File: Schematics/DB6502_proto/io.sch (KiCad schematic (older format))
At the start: 21 parts, among them J7 UART A, J8 UART_A, U17 SC26C92, U18 FT230XS, U4 74AC04, Y2 3,6864MHz

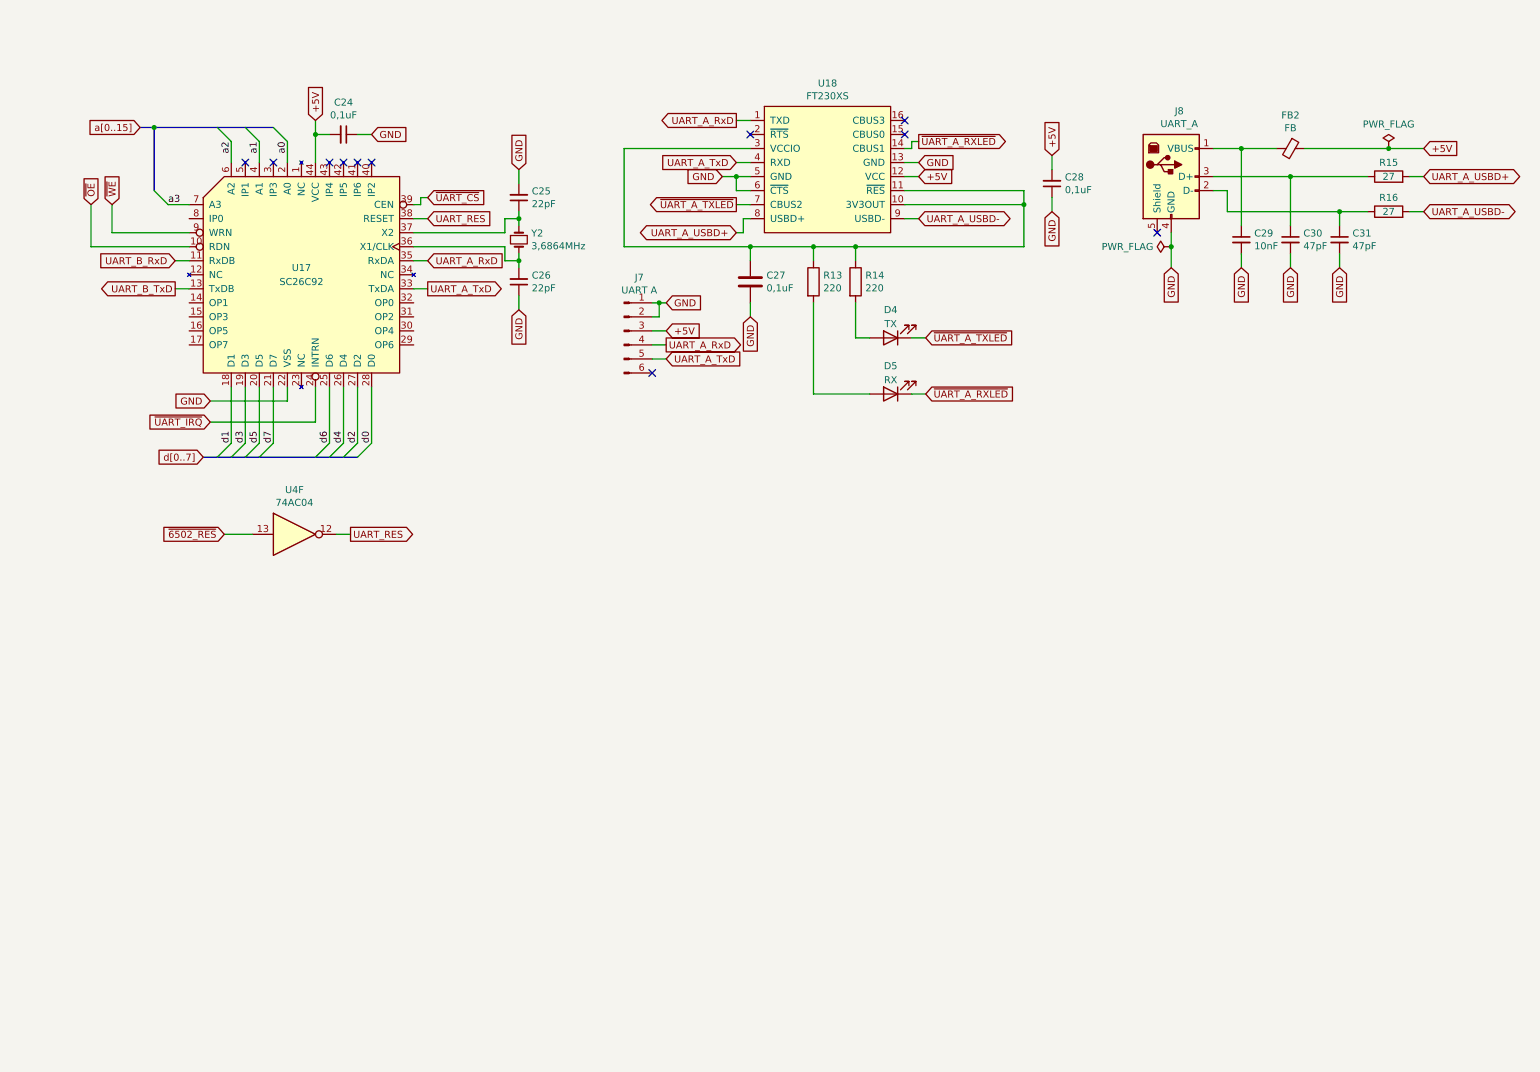
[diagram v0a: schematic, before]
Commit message: Improved layout of the I/O schematic
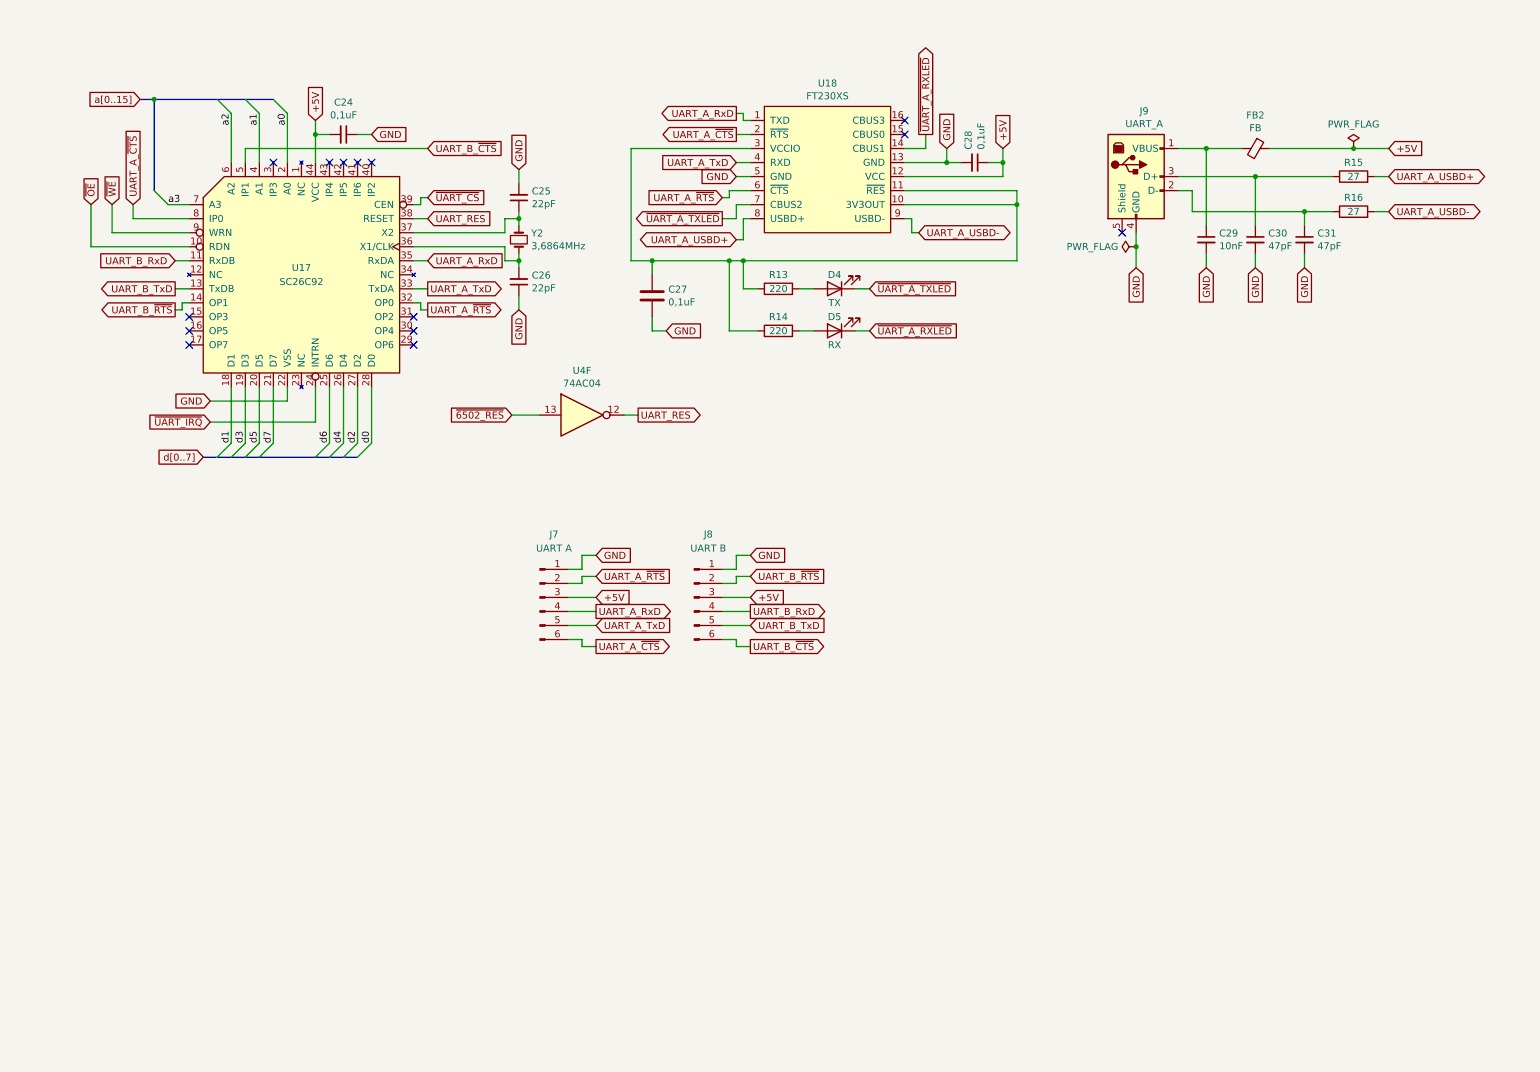
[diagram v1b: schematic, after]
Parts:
- removed R13: 220, Resistor_THT:R_Axial_DIN0207_L6.3mm_D2.5mm_P10.16mm_Horizontal, symbol Device:R
- added J8: UART B, Connector_PinHeader_2.54mm:PinHeader_1x06_P2.54mm_Horizontal, symbol Connector:Conn_01x06_Male
- added R14: 220, Resistor_THT:R_Axial_DIN0207_L6.3mm_D2.5mm_P10.16mm_Horizontal, symbol Device:R
- renumbered J8 to J9, R14 to R13
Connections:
- net +5V: now also C28.1, J8.3 (Pin_3); no longer C28.2
- net GND: now also C28.2, J8.1 (Pin_1); no longer C28.1, J7.2 (Pin_2), U18.6 (~CTS)
- net UART_B_RxD: now also J8.4 (Pin_4)
- net UART_B_TxD: now also J8.5 (Pin_5)
- net UART_B_~RTS: now reaches U17.14 (OP1)
- net UART_B_~RTS: now also J8.2 (Pin_2)
- net UART_A_~RTS: now reaches U17.32 (OP0)
- net UART_A_~RTS: now also J7.2 (Pin_2), U18.6 (~CTS)
- net UART_B_~CTS: now reaches U17.5 (IP1)
- net UART_B_~CTS: now also J8.6 (Pin_6)
- net UART_A_~CTS: now reaches U17.8 (IP0)
- net UART_A_~CTS: now also J7.6 (Pin_6), U18.2 (~RTS)
- net at C27.1, R13.1, U18.10 (3V3OUT)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: now also R14.1
- net at D5.2 (A): now also R14.2
- no-connect marks 11 -> 14
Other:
- moved on the sheet: C27, C28, C29, C30, C31, D4, D5, FB2, J7, J9, R13, R15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

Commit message: Fixed issue with UART CEN during low clock, added IRQ gate
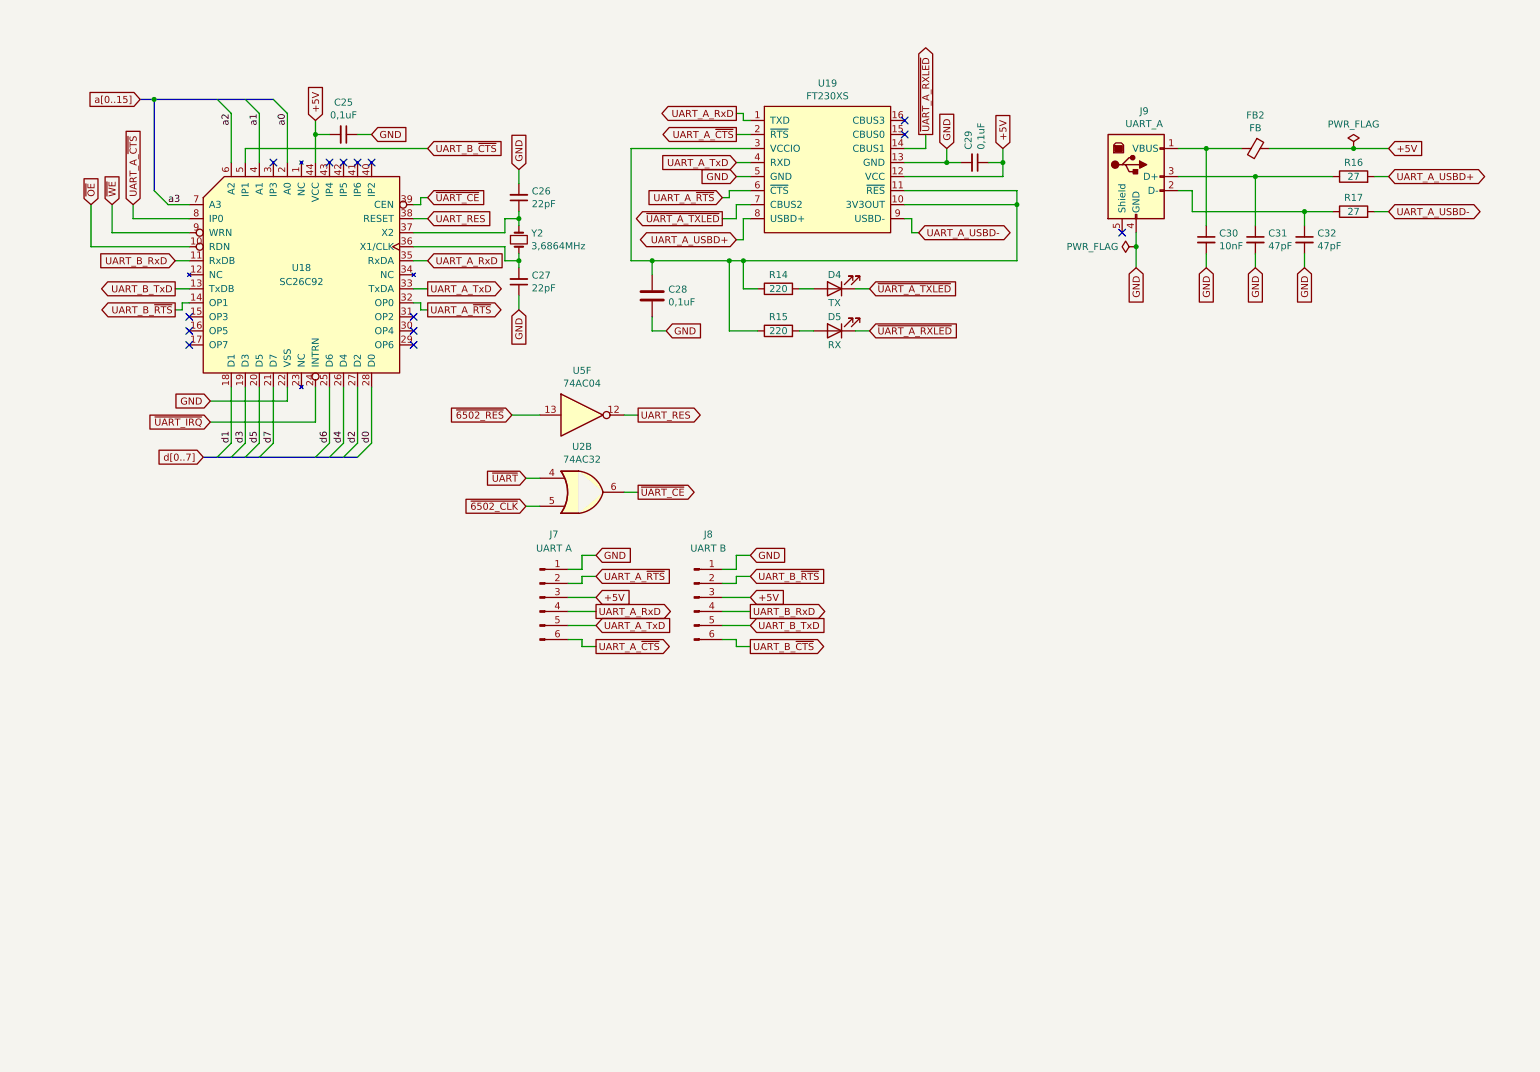
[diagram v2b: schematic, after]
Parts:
- added U2: 74AC32, symbol 74xx:74LS32
- renumbered C24 to C25, C25 to C26, C26 to C27, C27 to C28, C28 to C29, C29 to C30, C30 to C31, C31 to C32, R13 to R14, R14 to R15, R15 to R16, R16 to R17, U17 to U18, U18 to U19, U4 to U5
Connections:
- net ~UART_CS renamed ~UART_CE
- net ~UART_CE: now also U2.6
- new net ~6502_CLK: U2.5
- new net ~UART: U2.4
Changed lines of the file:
@@
 $EndDescr
 $Comp
-L 6502:SC26C92 U17
+L 6502:SC26C92 U18
 U 1 1 5F92CA23
 P 2400 2050
-F 0 "U17" H 2400 2100 50  0000 C CNN
+F 0 "U18" H 2400 2100 50  0000 C CNN
 F 1 "SC26C92" H 2400 2000 50  0000 C CNN
 F 2 "" H 2400 2050 50  0001 C CNN
@@
 	2500 950  2500 1050
 $Comp
-L Device:C_Small C24
+L Device:C_Small C25
 U 1 1 5F932BB1
 P 2700 1050
-F 0 "C24" V 2471 1050 50  0000 C CNN
+F 0 "C25" V 2471 1050 50  0000 C CNN
 F 1 "0,1uF" V 2562 1050 50  0000 C CNN
 F 2 "" H 2700 1050 50  0001 C CNN
@@
 UART_RES
 Text GLabel 3300 1500 2    50   Input ~ 0
-~UART_CS
+~UART_CE
 Wire Wire Line
 	3200 1650 3300 1650
@@
 $EndComp
 $Comp
-L Device:C_Small C25
+L Device:C_Small C26
 U 1 1 5F93E98E
 P 3950 1500
-F 0 "C25" H 3858 1454 50  0000 R CNN
+F 0 "C26" H 3858 1454 50  0000 R CNN
 F 1 "22pF" H 3858 1545 50  0000 R CNN
 F 2 "" H 3950 1500 50  0001 C CNN
@@
 $EndComp
 $Comp
-L Device:C_Small C26
+L Device:C_Small C27
 U 1 1 5F93F1BF
 P 3950 2100
-F 0 "C26" H 3858 2054 50  0000 R CNN
+F 0 "C27" H 3858 2054 50  0000 R CNN
 F 1 "22pF" H 3858 2145 50  0000 R CNN
 F 2 "" H 3950 2100 50  0001 C CNN
@@
 AR Path="/6014B4D9/5F95BFD2" Ref="U?"  Part="1"
 AR Path="/5F8F4E1E/5F95BFD2" Ref="U?"  Part="1"
-AR Path="/5F910E81/5F95BFD2" Ref="U18"  Part="1"
-F 0 "U18" H 6150 1915 50  0000 C CNN
+AR Path="/5F910E81/5F95BFD2" Ref="U19"  Part="1"
+F 0 "U19" H 6150 1915 50  0000 C CNN
 F 1 "FT230XS" H 6150 1824 50  0000 C CNN
 F 2 "Package_SO:SSOP-16_5.3x6.2mm_P0.65mm" H 6150 1800 50  0001 C CNN
@@
 AR Path="/6014B4D9/5F95BFF2" Ref="C?"  Part="1"
 AR Path="/5F8F4E1E/5F95BFF2" Ref="C?"  Part="1"
-AR Path="/5F910E81/5F95BFF2" Ref="C27"  Part="1"
-F 0 "C27" H 5015 2246 50  0000 L CNN
+AR Path="/5F910E81/5F95BFF2" Ref="C28"  Part="1"
+F 0 "C28" H 5015 2246 50  0000 L CNN
 F 1 "0,1uF" H 5015 2155 50  0000 L CNN
 F 2 "Capacitor_THT:C_Disc_D5.0mm_W2.5mm_P2.50mm" H 4938 2050 50  0001 C CNN
@@
 AR Path="/6014B4D9/5F95C00C" Ref="R?"  Part="1"
 AR Path="/5F8F4E1E/5F95C00C" Ref="R?"  Part="1"
-AR Path="/5F910E81/5F95C00C" Ref="R13"  Part="1"
-F 0 "R13" V 5900 2150 50  0000 C CNN
+AR Path="/5F910E81/5F95C00C" Ref="R14"  Part="1"
+F 0 "R14" V 5900 2150 50  0000 C CNN
 F 1 "220" V 5800 2150 50  0000 C CNN
 F 2 "Resistor_THT:R_Axial_DIN0207_L6.3mm_D2.5mm_P10.16mm_Horizontal" V 5730 2150 50  0001 C CNN
@@
 P 7200 1250
 AR Path="/5F8F4E1E/5F95C03D" Ref="C?"  Part="1"
-AR Path="/5F910E81/5F95C03D" Ref="C28"  Part="1"
-F 0 "C28" H 7108 1204 50  0000 R CNN
+AR Path="/5F910E81/5F95C03D" Ref="C29"  Part="1"
+F 0 "C29" H 7108 1204 50  0000 R CNN
 F 1 "0,1uF" H 7108 1295 50  0000 R CNN
 F 2 "" H 7200 1250 50  0001 C CNN
@@
 AR Path="/6014B4D9/5F982929" Ref="R?"  Part="1"
 AR Path="/5F8F4E1E/5F982929" Ref="R?"  Part="1"
-AR Path="/5F910E81/5F982929" Ref="R16"  Part="1"
-F 0 "R16" V 10000 1600 50  0000 C CNN
+AR Path="/5F910E81/5F982929" Ref="R17"  Part="1"
+F 0 "R17" V 10000 1600 50  0000 C CNN
 F 1 "27" V 9900 1600 50  0000 C CNN
 F 2 "Resistor_THT:R_Axial_DIN0207_L6.3mm_D2.5mm_P10.16mm_Horizontal" V 9830 1600 50  0001 C CNN
@@
 AR Path="/6014B4D9/5F98292F" Ref="R?"  Part="1"
 AR Path="/5F8F4E1E/5F98292F" Ref="R?"  Part="1"
-AR Path="/5F910E81/5F98292F" Ref="R15"  Part="1"
-F 0 "R15" V 10000 1350 50  0000 C CNN
+AR Path="/5F910E81/5F98292F" Ref="R16"  Part="1"
+F 0 "R16" V 10000 1350 50  0000 C CNN
 F 1 "27" V 9900 1350 50  0000 C CNN
 F 2 "Resistor_THT:R_Axial_DIN0207_L6.3mm_D2.5mm_P10.16mm_Horizontal" V 9830 1350 50  0001 C CNN
@@
 AR Path="/6014B4D9/5F982938" Ref="C?"  Part="1"
 AR Path="/5F8F4E1E/5F982938" Ref="C?"  Part="1"
-AR Path="/5F910E81/5F982938" Ref="C30"  Part="1"
-F 0 "C30" H 9292 1846 50  0000 L CNN
+AR Path="/5F910E81/5F982938" Ref="C31"  Part="1"
+F 0 "C31" H 9292 1846 50  0000 L CNN
 F 1 "47pF" H 9292 1755 50  0000 L CNN
 F 2 "Capacitor_THT:C_Disc_D5.0mm_W2.5mm_P2.50mm" H 9200 1800 50  0001 C CNN
@@
 AR Path="/6014B4D9/5F98293E" Ref="C?"  Part="1"
 AR Path="/5F8F4E1E/5F98293E" Ref="C?"  Part="1"
-AR Path="/5F910E81/5F98293E" Ref="C31"  Part="1"
-F 0 "C31" H 9642 1846 50  0000 L CNN
+AR Path="/5F910E81/5F98293E" Ref="C32"  Part="1"
+F 0 "C32" H 9642 1846 50  0000 L CNN
 F 1 "47pF" H 9642 1755 50  0000 L CNN
 F 2 "Capacitor_THT:C_Disc_D5.0mm_W2.5mm_P2.50mm" H 9550 1800 50  0001 C CNN
@@
 AR Path="/6014B4D9/5F982950" Ref="C?"  Part="1"
 AR Path="/5F8F4E1E/5F982950" Ref="C?"  Part="1"
-AR Path="/5F910E81/5F982950" Ref="C29"  Part="1"
-F 0 "C29" H 8942 1846 50  0000 L CNN
+AR Path="/5F910E81/5F982950" Ref="C30"  Part="1"
+F 0 "C30" H 8942 1846 50  0000 L CNN
 F 1 "10nF" H 8942 1755 50  0000 L CNN
 F 2 "Capacitor_THT:C_Disc_D5.0mm_W2.5mm_P2.50mm" H 8850 1800 50  0001 C CNN
@@
 P 4400 3050
 AR Path="/5F8F4E1E/5F9A15C7" Ref="U?"  Part="6"
-AR Path="/5F910E81/5F9A15C7" Ref="U4"  Part="6"
-F 0 "U4" H 4400 3367 50  0000 C CNN
+AR Path="/5F910E81/5F9A15C7" Ref="U5"  Part="6"
+F 0 "U5" H 4400 3367 50  0000 C CNN
 F 1 "74AC04" H 4400 3276 50  0000 C CNN
 F 2 "" H 4400 3050 50  0001 C CNN
@@
 AR Path="/6014B4D9/5FA78290" Ref="R?"  Part="1"
 AR Path="/5F8F4E1E/5FA78290" Ref="R?"  Part="1"
-AR Path="/5F910E81/5FA78290" Ref="R14"  Part="1"
-F 0 "R14" V 5900 2450 50  0000 C CNN
+AR Path="/5F910E81/5FA78290" Ref="R15"  Part="1"
+F 0 "R15" V 5900 2450 50  0000 C CNN
 F 1 "220" V 5800 2450 50  0000 C CNN
 F 2 "Resistor_THT:R_Axial_DIN0207_L6.3mm_D2.5mm_P10.16mm_Horizontal" V 5730 2450 50  0001 C CNN
@@
 Wire Wire Line
 	6750 1650 6700 1650
+Text GLabel 4000 3500 0    50   Input ~ 0
+~UART
+Text GLabel 4000 3700 0    50   Input ~ 0
+~6502_CLK
+Wire Wire Line
+	4000 3700 4100 3700
+Wire Wire Line
+	4000 3500 4100 3500
+Text GLabel 4800 3600 2    50   Output ~ 0
+~UART_CE
+$Comp
+L 74xx:74LS32 U?
+U 2 1 5FAF5A36
+P 4400 3600
+AR Path="/5FAF5A36" Ref="U?"  Part="2"
+AR Path="/5F910E81/5FAF5A36" Ref="U2"  Part="2"
+F 0 "U2" H 4400 3925 50  0000 C CNN
+F 1 "74AC32" H 4400 3834 50  0000 C CNN
+F 2 "" H 4400 3600 50  0001 C CNN
+F 3 "http://www.ti.com/lit/gpn/sn74LS32" H 4400 3600 50  0001 C CNN
+	2    4400 3600
+	1    0    0    -1
+$EndComp
+Wire Wire Line
+	4700 3600 4800 3600
 Wire Bus Line
 	1350 800  2200 800
